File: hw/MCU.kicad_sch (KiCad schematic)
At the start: 13 parts

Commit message: annotations
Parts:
- gave numbers to parts that had none: 13
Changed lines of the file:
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@@
   (symbol (lib_id "Device:C") (at 241.3 26.67 0) (unit 1)
     (in_bom yes) (on_board yes) (dnp no) (fields_autoplaced)
-    (property "Reference" "C?" (at 245.11 25.4 0)
+    (property "Reference" "C6" (at 245.11 25.4 0)
       (effects (font (size 1.27 1.27)) (justify left))
     )
@@
       (project "KiConSZ2023"
         (path "/8659c260-f029-4e72-8b9a-85fff45eea40/aebeadc6-0cb2-44f8-88a5-80ae76b1b2bc"
-          (reference "C?") (unit 1)
+          (reference "C6") (unit 1)
         )
       )
@@
   (symbol (lib_id "Switch:SW_Push") (at 254 142.24 0) (unit 1)
     (in_bom yes) (on_board yes) (dnp no) (fields_autoplaced)
-    (property "Reference" "SW?" (at 254 134.62 0)
+    (property "Reference" "SW3" (at 254 134.62 0)
       (effects (font (size 1.27 1.27)))
     )
@@
       (project "KiConSZ2023"
         (path "/8659c260-f029-4e72-8b9a-85fff45eea40/aebeadc6-0cb2-44f8-88a5-80ae76b1b2bc"
-          (reference "SW?") (unit 1)
+          (reference "SW3") (unit 1)
         )
       )
@@
   (symbol (lib_id "Device:R") (at 264.16 149.86 0) (unit 1)
     (in_bom yes) (on_board yes) (dnp no) (fields_autoplaced)
-    (property "Reference" "R?" (at 266.7 148.59 0)
+    (property "Reference" "R3" (at 266.7 148.59 0)
       (effects (font (size 1.27 1.27)) (justify left))
     )
@@
       (project "KiConSZ2023"
         (path "/8659c260-f029-4e72-8b9a-85fff45eea40/aebeadc6-0cb2-44f8-88a5-80ae76b1b2bc"
-          (reference "R?") (unit 1)
+          (reference "R3") (unit 1)
         )
       )
@@
   (symbol (lib_id "Switch:SW_Push") (at 254 111.76 90) (unit 1)
     (in_bom yes) (on_board yes) (dnp no) (fields_autoplaced)
-    (property "Reference" "SW?" (at 255.27 110.49 90)
+    (property "Reference" "SW2" (at 255.27 110.49 90)
       (effects (font (size 1.27 1.27)) (justify right))
     )
@@
       (project "KiConSZ2023"
         (path "/8659c260-f029-4e72-8b9a-85fff45eea40/aebeadc6-0cb2-44f8-88a5-80ae76b1b2bc"
-          (reference "SW?") (unit 1)
+          (reference "SW2") (unit 1)
         )
       )
@@
   (symbol (lib_id "power:GND") (at 114.3 177.8 0) (unit 1)
     (in_bom yes) (on_board yes) (dnp no) (fields_autoplaced)
-    (property "Reference" "#PWR?" (at 114.3 184.15 0)
+    (property "Reference" "#PWR03" (at 114.3 184.15 0)
       (effects (font (size 1.27 1.27)) hide)
     )
@@
       (project "KiConSZ2023"
         (path "/8659c260-f029-4e72-8b9a-85fff45eea40/aebeadc6-0cb2-44f8-88a5-80ae76b1b2bc"
-          (reference "#PWR?") (unit 1)
+          (reference "#PWR03") (unit 1)
         )
       )
@@
   (symbol (lib_id "power:GND") (at 264.16 157.48 0) (unit 1)
     (in_bom yes) (on_board yes) (dnp no) (fields_autoplaced)
-    (property "Reference" "#PWR?" (at 264.16 163.83 0)
+    (property "Reference" "#PWR05" (at 264.16 163.83 0)
       (effects (font (size 1.27 1.27)) hide)
     )
@@
       (project "KiConSZ2023"
         (path "/8659c260-f029-4e72-8b9a-85fff45eea40/aebeadc6-0cb2-44f8-88a5-80ae76b1b2bc"
-          (reference "#PWR?") (unit 1)
+          (reference "#PWR05") (unit 1)
         )
       )
@@
   (symbol (lib_id "power:GND") (at 254 121.92 0) (unit 1)
     (in_bom yes) (on_board yes) (dnp no) (fields_autoplaced)
-    (property "Reference" "#PWR?" (at 254 128.27 0)
+    (property "Reference" "#PWR04" (at 254 128.27 0)
       (effects (font (size 1.27 1.27)) hide)
     )
@@
       (project "KiConSZ2023"
         (path "/8659c260-f029-4e72-8b9a-85fff45eea40/aebeadc6-0cb2-44f8-88a5-80ae76b1b2bc"
-          (reference "#PWR?") (unit 1)
+          (reference "#PWR04") (unit 1)
         )
       )
@@
   (symbol (lib_id "power:VDD") (at 40.64 26.67 0) (unit 1)
     (in_bom yes) (on_board yes) (dnp no)
-    (property "Reference" "#PWR?" (at 40.64 30.48 0)
+    (property "Reference" "#PWR02" (at 40.64 30.48 0)
       (effects (font (size 1.27 1.27)) hide)
     )
@@
       (project "KiConSZ2023"
         (path "/8659c260-f029-4e72-8b9a-85fff45eea40/aebeadc6-0cb2-44f8-88a5-80ae76b1b2bc"
-          (reference "#PWR?") (unit 1)
+          (reference "#PWR02") (unit 1)
         )
       )
@@
   (symbol (lib_id "Device:C") (at 266.7 111.76 0) (unit 1)
     (in_bom yes) (on_board yes) (dnp no) (fields_autoplaced)
-    (property "Reference" "C?" (at 270.51 110.49 0)
+    (property "Reference" "C9" (at 270.51 110.49 0)
       (effects (font (size 1.27 1.27)) (justify left))
     )
@@
       (project "KiConSZ2023"
         (path "/8659c260-f029-4e72-8b9a-85fff45eea40/aebeadc6-0cb2-44f8-88a5-80ae76b1b2bc"
-          (reference "C?") (unit 1)
+          (reference "C9") (unit 1)
         )
       )
@@
   (symbol (lib_id "Device:C") (at 181.61 26.67 0) (unit 1)
     (in_bom yes) (on_board yes) (dnp no) (fields_autoplaced)
-    (property "Reference" "C?" (at 185.42 25.4 0)
+    (property "Reference" "C3" (at 185.42 25.4 0)
       (effects (font (size 1.27 1.27)) (justify left))
     )
@@
       (project "KiConSZ2023"
         (path "/8659c260-f029-4e72-8b9a-85fff45eea40/aebeadc6-0cb2-44f8-88a5-80ae76b1b2bc"
-          (reference "C?") (unit 1)
+          (reference "C3") (unit 1)
         )
       )
@@
   (symbol (lib_id "Device:C") (at 227.33 26.67 0) (unit 1)
     (in_bom yes) (on_board yes) (dnp no) (fields_autoplaced)
-    (property "Reference" "C?" (at 231.14 25.4 0)
+    (property "Reference" "C5" (at 231.14 25.4 0)
       (effects (font (size 1.27 1.27)) (justify left))
     )
@@
       (project "KiConSZ2023"
         (path "/8659c260-f029-4e72-8b9a-85fff45eea40/aebeadc6-0cb2-44f8-88a5-80ae76b1b2bc"
-          (reference "C?") (unit 1)
+          (reference "C5") (unit 1)
         )
       )
@@
   (symbol (lib_id "Device:R") (at 254 96.52 0) (unit 1)
     (in_bom yes) (on_board yes) (dnp no) (fields_autoplaced)
-    (property "Reference" "R?" (at 256.54 95.25 0)
+    (property "Reference" "R2" (at 256.54 95.25 0)
       (effects (font (size 1.27 1.27)) (justify left))
     )
@@
       (project "KiConSZ2023"
         (path "/8659c260-f029-4e72-8b9a-85fff45eea40/aebeadc6-0cb2-44f8-88a5-80ae76b1b2bc"
-          (reference "R?") (unit 1)
+          (reference "R2") (unit 1)
         )
       )
@@
   (symbol (lib_id "Device:C") (at 193.04 26.67 0) (unit 1)
     (in_bom yes) (on_board yes) (dnp no) (fields_autoplaced)
-    (property "Reference" "C?" (at 196.85 25.4 0)
+    (property "Reference" "C4" (at 196.85 25.4 0)
       (effects (font (size 1.27 1.27)) (justify left))
     )
@@
       (project "KiConSZ2023"
         (path "/8659c260-f029-4e72-8b9a-85fff45eea40/aebeadc6-0cb2-44f8-88a5-80ae76b1b2bc"
-          (reference "C?") (unit 1)
+          (reference "C4") (unit 1)
         )
       )
@@
   (symbol (lib_id "IotPi_MCU_nationstech:N32L40xRyLz") (at 157.48 99.06 0) (unit 1)
     (in_bom yes) (on_board yes) (dnp no)
-    (property "Reference" "U?" (at 157.48 96.52 0)
+    (property "Reference" "U2" (at 157.48 96.52 0)
       (effects (font (size 1.27 1.27)))
     )
@@
       (project "KiConSZ2023"
         (path "/8659c260-f029-4e72-8b9a-85fff45eea40/aebeadc6-0cb2-44f8-88a5-80ae76b1b2bc"
-          (reference "U?") (unit 1)
+          (reference "U2") (unit 1)
         )
       )
@@
   (symbol (lib_id "Device:C") (at 254 26.67 0) (unit 1)
     (in_bom yes) (on_board yes) (dnp no) (fields_autoplaced)
-    (property "Reference" "C?" (at 257.81 25.4 0)
+    (property "Reference" "C7" (at 257.81 25.4 0)
       (effects (font (size 1.27 1.27)) (justify left))
     )
@@
       (project "KiConSZ2023"
         (path "/8659c260-f029-4e72-8b9a-85fff45eea40/aebeadc6-0cb2-44f8-88a5-80ae76b1b2bc"
-          (reference "C?") (unit 1)
+          (reference "C7") (unit 1)
         )
       )
@@
   (symbol (lib_id "Device:C") (at 168.91 26.67 0) (unit 1)
     (in_bom yes) (on_board yes) (dnp no) (fields_autoplaced)
-    (property "Reference" "C?" (at 172.72 25.4 0)
+    (property "Reference" "C2" (at 172.72 25.4 0)
       (effects (font (size 1.27 1.27)) (justify left))
     )
@@
       (project "KiConSZ2023"
         (path "/8659c260-f029-4e72-8b9a-85fff45eea40/aebeadc6-0cb2-44f8-88a5-80ae76b1b2bc"
-          (reference "C?") (unit 1)
+          (reference "C2") (unit 1)
         )
       )
@@
   (symbol (lib_id "Device:C") (at 266.7 26.67 0) (unit 1)
     (in_bom yes) (on_board yes) (dnp no) (fields_autoplaced)
-    (property "Reference" "C?" (at 270.51 25.4 0)
+    (property "Reference" "C8" (at 270.51 25.4 0)
       (effects (font (size 1.27 1.27)) (justify left))
     )
@@
       (project "KiConSZ2023"
         (path "/8659c260-f029-4e72-8b9a-85fff45eea40/aebeadc6-0cb2-44f8-88a5-80ae76b1b2bc"
-          (reference "C?") (unit 1)
-        )
-      )
+          (reference "C8") (unit 1)
+        )
+      )

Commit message: updated footprint of N32L406
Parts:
- U2: footprint (none) -> Package_QFP:LQFP-64_10x10mm_P0.5mm
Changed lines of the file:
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@@
       (effects (font (size 1.27 1.27)))
     )
-    (property "Footprint" "" (at 157.48 106.68 0)
+    (property "Footprint" "Package_QFP:LQFP-64_10x10mm_P0.5mm" (at 157.48 106.68 0)
       (effects (font (size 1.27 1.27)) hide)
     )

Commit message: updated LCSC of switches
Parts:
- SW2, SW3: LCSC (none) -> C139797; Vendor (none) -> ALPSALPINE(阿尔卑斯阿尔派); Vendor Model (none) -> SKRPACE010
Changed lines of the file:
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@@
       (effects (font (size 1.27 1.27)) hide)
     )
-    (property "Description" "" (at 254 142.24 0)
+    (property "Description" "触点电流: 50mA 额定电压(DC): 16V 电路结构: 单刀单掷 安装方式: 立贴 按钮形状: 椭圆形按钮 带灯: - 机械寿命:" (at 254 142.24 0)
       (effects (font (size 1.27 1.27)) hide)
     )
-    (property "LCSC" "" (at 254 142.24 0)
+    (property "LCSC" "C139797" (at 254 142.24 0)
       (effects (font (size 1.27 1.27)) hide)
     )
-    (property "Vendor" "" (at 254 142.24 0)
+    (property "Vendor" "ALPSALPINE(阿尔卑斯阿尔派)" (at 254 142.24 0)
       (effects (font (size 1.27 1.27)) hide)
     )
-    (property "Vendor Model" "" (at 254 142.24 0)
+    (property "Vendor Model" "SKRPACE010" (at 254 142.24 0)
       (effects (font (size 1.27 1.27)) hide)
     )
@@
       (effects (font (size 1.27 1.27)) hide)
     )
-    (property "Description" "" (at 254 111.76 0)
+    (property "Description" "触点电流: 50mA 额定电压(DC): 16V 电路结构: 单刀单掷 安装方式: 立贴 按钮形状: 椭圆形按钮 带灯: - 机械寿命:" (at 254 111.76 0)
       (effects (font (size 1.27 1.27)) hide)
     )
-    (property "LCSC" "" (at 254 111.76 0)
+    (property "LCSC" "C139797" (at 254 111.76 0)
       (effects (font (size 1.27 1.27)) hide)
     )
-    (property "Vendor" "" (at 254 111.76 0)
+    (property "Vendor" "ALPSALPINE(阿尔卑斯阿尔派)" (at 254 111.76 0)
       (effects (font (size 1.27 1.27)) hide)
     )
-    (property "Vendor Model" "" (at 254 111.76 0)
+    (property "Vendor Model" "SKRPACE010" (at 254 111.76 0)
       (effects (font (size 1.27 1.27)) hide)
     )

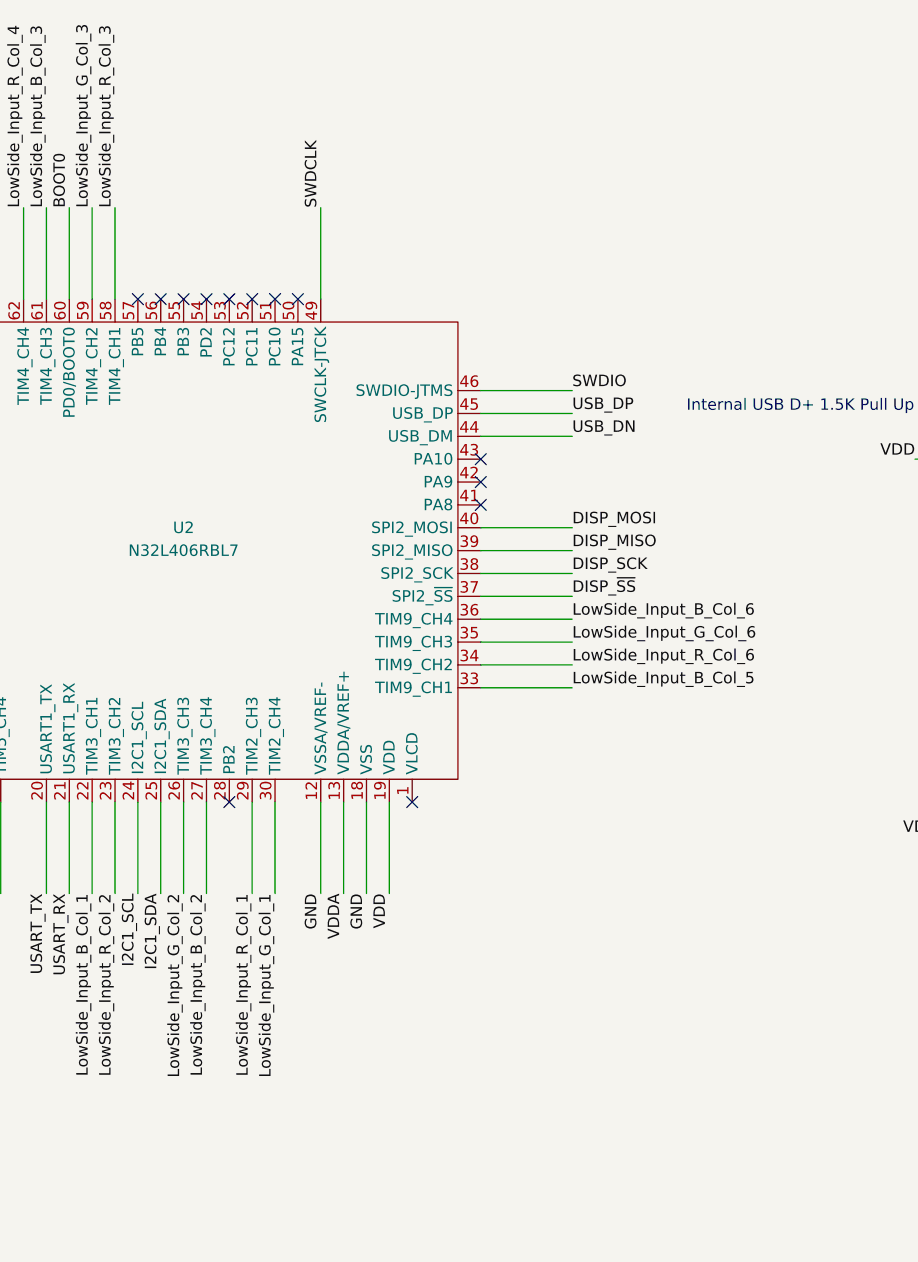
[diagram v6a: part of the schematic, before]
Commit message: fix issues in schematic and footprints
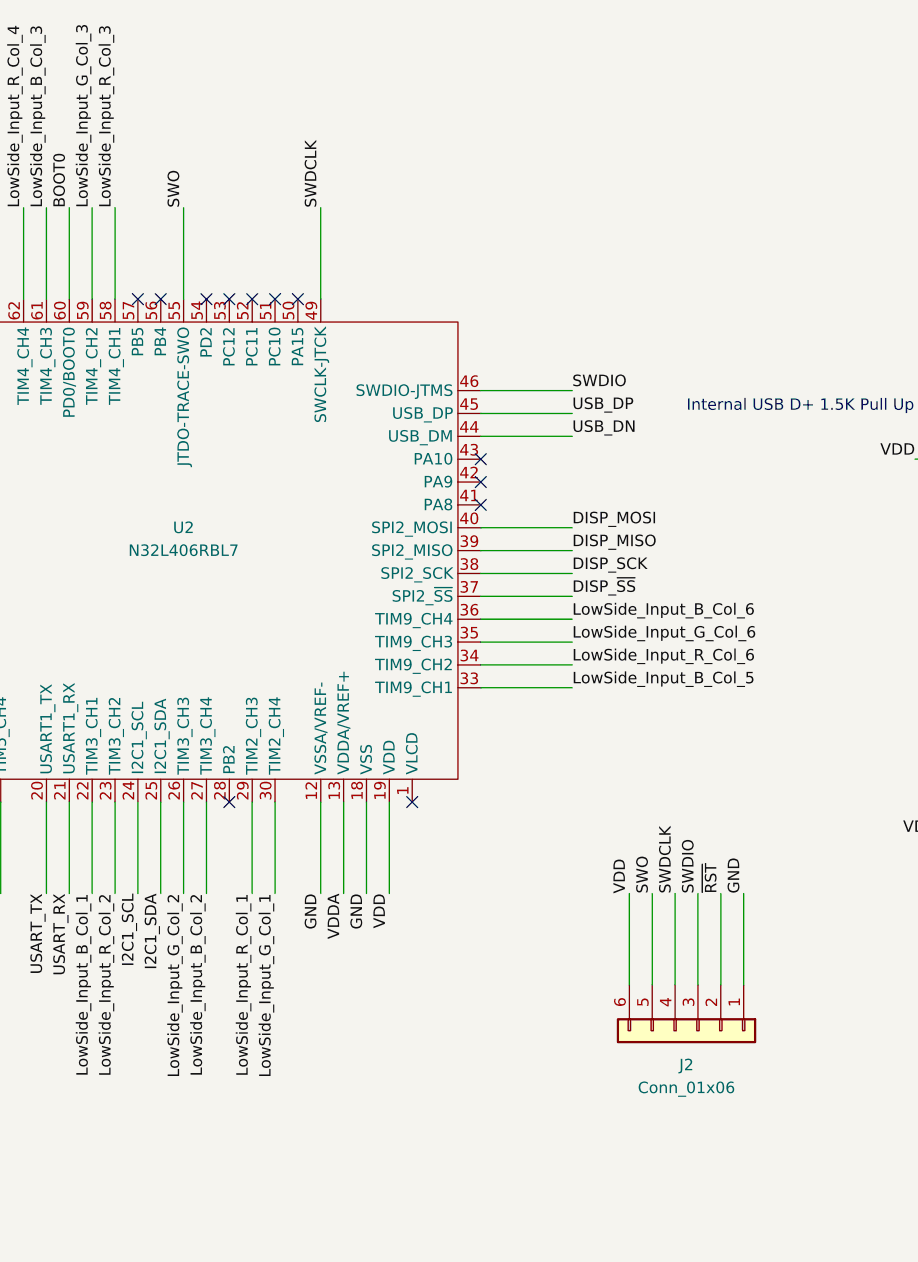
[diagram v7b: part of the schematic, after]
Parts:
- added J2: Conn_01x06, Connector_PinHeader_2.54mm:PinHeader_1x06_P2.54mm_Vertical, symbol Connector_Generic:Conn_01x06
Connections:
- net GND: now also J2.1 (Pin_1)
- net SWDCLK: now also J2.4 (Pin_4)
- net SWDIO: now also J2.3 (Pin_3)
- net VDD: now also J2.6 (Pin_6)
- net ~{RST}: now also J2.2 (Pin_2)
- net SWO: now reaches U2.55 (PB3)
- net SWO: now also J2.5 (Pin_5)
- no-connect marks 14 -> 13
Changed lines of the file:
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@@
   (no_connect (at 167.64 71.12))
   (no_connect (at 162.56 127))
-  (no_connect (at 157.48 71.12))
   (no_connect (at 152.4 71.12))
   (no_connect (at 165.1 71.12))
@@
     (stroke (width 0) (type default))
   )
+  (wire (pts (xy 209.55 147.32) (xy 209.55 137.16))
+    (stroke (width 0) (type default))
+  )
   (wire (pts (xy 43.18 165.1) (xy 53.34 165.1))
     (stroke (width 0) (type default))
@@
     (stroke (width 0) (type default))
   )
+  (wire (pts (xy 157.48 71.12) (xy 157.48 60.96))
+    (stroke (width 0) (type default))
+  )
   (wire (pts (xy 114.3 172.72) (xy 114.3 177.8))
     (stroke (width 0) (type default))
@@
     (stroke (width 0) (type default))
   )
+  (wire (pts (xy 217.17 137.16) (xy 217.17 147.32))
+    (stroke (width 0) (type default))
+  )
   (wire (pts (xy 43.18 119.38) (xy 53.34 119.38))
     (stroke (width 0) (type default))
@@
     (stroke (width 0) (type default))
   )
+  (wire (pts (xy 214.63 147.32) (xy 214.63 137.16))
+    (stroke (width 0) (type default))
+  )
   (wire (pts (xy 43.18 157.48) (xy 53.34 157.48))
     (stroke (width 0) (type default))
@@
     (stroke (width 0) (type default))
   )
+  (wire (pts (xy 219.71 137.16) (xy 219.71 147.32))
+    (stroke (width 0) (type default))
+  )
   (wire (pts (xy 144.78 60.96) (xy 144.78 71.12))
     (stroke (width 0) (type default))
@@
     (stroke (width 0) (type default))
   )
+  (wire (pts (xy 207.01 147.32) (xy 207.01 137.16))
+    (stroke (width 0) (type default))
+  )
   (wire (pts (xy 271.78 142.24) (xy 264.16 142.24))
     (stroke (width 0) (type default))
@@
   )
   (wire (pts (xy 124.46 114.3) (xy 114.3 114.3))
+    (stroke (width 0) (type default))
+  )
+  (wire (pts (xy 212.09 147.32) (xy 212.09 137.16))
     (stroke (width 0) (type default))
   )
@@
     (effects (font (size 1.27 1.27)) (justify left bottom))
   )
+  (label "~{RST}" (at 217.17 137.16 90) (fields_autoplaced)
+    (effects (font (size 1.27 1.27)) (justify left bottom))
+  )
   (label "USART_TX" (at 142.24 137.16 270) (fields_autoplaced)
     (effects (font (size 1.27 1.27)) (justify right bottom))
@@
     (effects (font (size 1.27 1.27)) (justify right bottom))
   )
+  (label "VDD" (at 207.01 137.16 90) (fields_autoplaced)
+    (effects (font (size 1.27 1.27)) (justify left bottom))
+  )
   (label "VDD" (at 241.3 130.81 180) (fields_autoplaced)
     (effects (font (size 1.27 1.27)) (justify right bottom))
@@
     (effects (font (size 1.27 1.27)) (justify right bottom))
   )
+  (label "SWO" (at 209.55 137.16 90) (fields_autoplaced)
+    (effects (font (size 1.27 1.27)) (justify left bottom))
+  )
   (label "GND" (at 177.8 137.16 270) (fields_autoplaced)
     (effects (font (size 1.27 1.27)) (justify right bottom))
@@
     (effects (font (size 1.27 1.27)) (justify left bottom))
   )
+  (label "GND" (at 219.71 137.16 90) (fields_autoplaced)
+    (effects (font (size 1.27 1.27)) (justify left bottom))
+  )
   (label "LowSide_Input_B_Col_1" (at 147.32 137.16 270) (fields_autoplaced)
     (effects (font (size 1.27 1.27)) (justify right bottom))
@@
     (effects (font (size 1.27 1.27)) (justify left bottom))
   )
+  (label "SWO" (at 157.48 60.96 90) (fields_autoplaced)
+    (effects (font (size 1.27 1.27)) (justify left bottom))
+  )
   (label "HighSide_Input_Row_5" (at 114.3 96.52 180) (fields_autoplaced)
     (effects (font (size 1.27 1.27)) (justify right bottom))
@@
     (effects (font (size 1.27 1.27)) (justify left bottom))
   )
+  (label "SWDCLK" (at 212.09 137.16 90) (fields_autoplaced)
+    (effects (font (size 1.27 1.27)) (justify left bottom))
+  )
   (label "HighSide_Input_Row_4" (at 114.3 91.44 180) (fields_autoplaced)
     (effects (font (size 1.27 1.27)) (justify right bottom))
+  )
+  (label "SWDIO" (at 214.63 137.16 90) (fields_autoplaced)
+    (effects (font (size 1.27 1.27)) (justify left bottom))
   )
   (label "GND" (at 172.72 137.16 270) (fields_autoplaced)
@@
     (pin "53")
     (pin "54")
-    (pin "55")
+    (pin "55" (alternate "JTDO-TRACE-SWO"))
     (pin "56")
     (pin "57")
@@
         )
       )
+    )
+  )
+  (symbol (lib_id "Connector_Generic:Conn_01x06") (at 214.63 152.4 270) (unit 1)
+    (in_bom yes) (on_board yes) (dnp no) (fields_autoplaced)
+    (property "Reference" "J2" (at 213.36 156.21 90)
+      (effects (font (size 1.27 1.27)))
+    )
+    (property "Value" "Conn_01x06" (at 213.36 158.75 90)
+      (effects (font (size 1.27 1.27)))
+    )
+    (property "Footprint" "Connector_PinHeader_2.54mm:PinHeader_1x06_P2.54mm_Vertical" (at 214.63 152.4 0)
+      (effects (font (size 1.27 1.27)) hide)
+    )
+    (property "Datasheet" "~" (at 214.63 152.4 0)
+      (effects (font (size 1.27 1.27)) hide)
+    )
+    (pin "1")
+    (pin "2")
+    (pin "3")
+    (pin "4")
+    (pin "5")
+    (pin "6")
+    (instances
+      (project "KiConSZ2023"
+        (path "/8659c260-f029-4e72-8b9a-85fff45eea40/aebeadc6-0cb2-44f8-88a5-80ae76b1b2bc"
+          (reference "J2") (unit 1)
+        )
+      )
